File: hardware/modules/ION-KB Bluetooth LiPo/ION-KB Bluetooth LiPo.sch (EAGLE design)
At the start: 4 parts, among them IC1 BLUETOOTH-RN42", U1 MCP73831

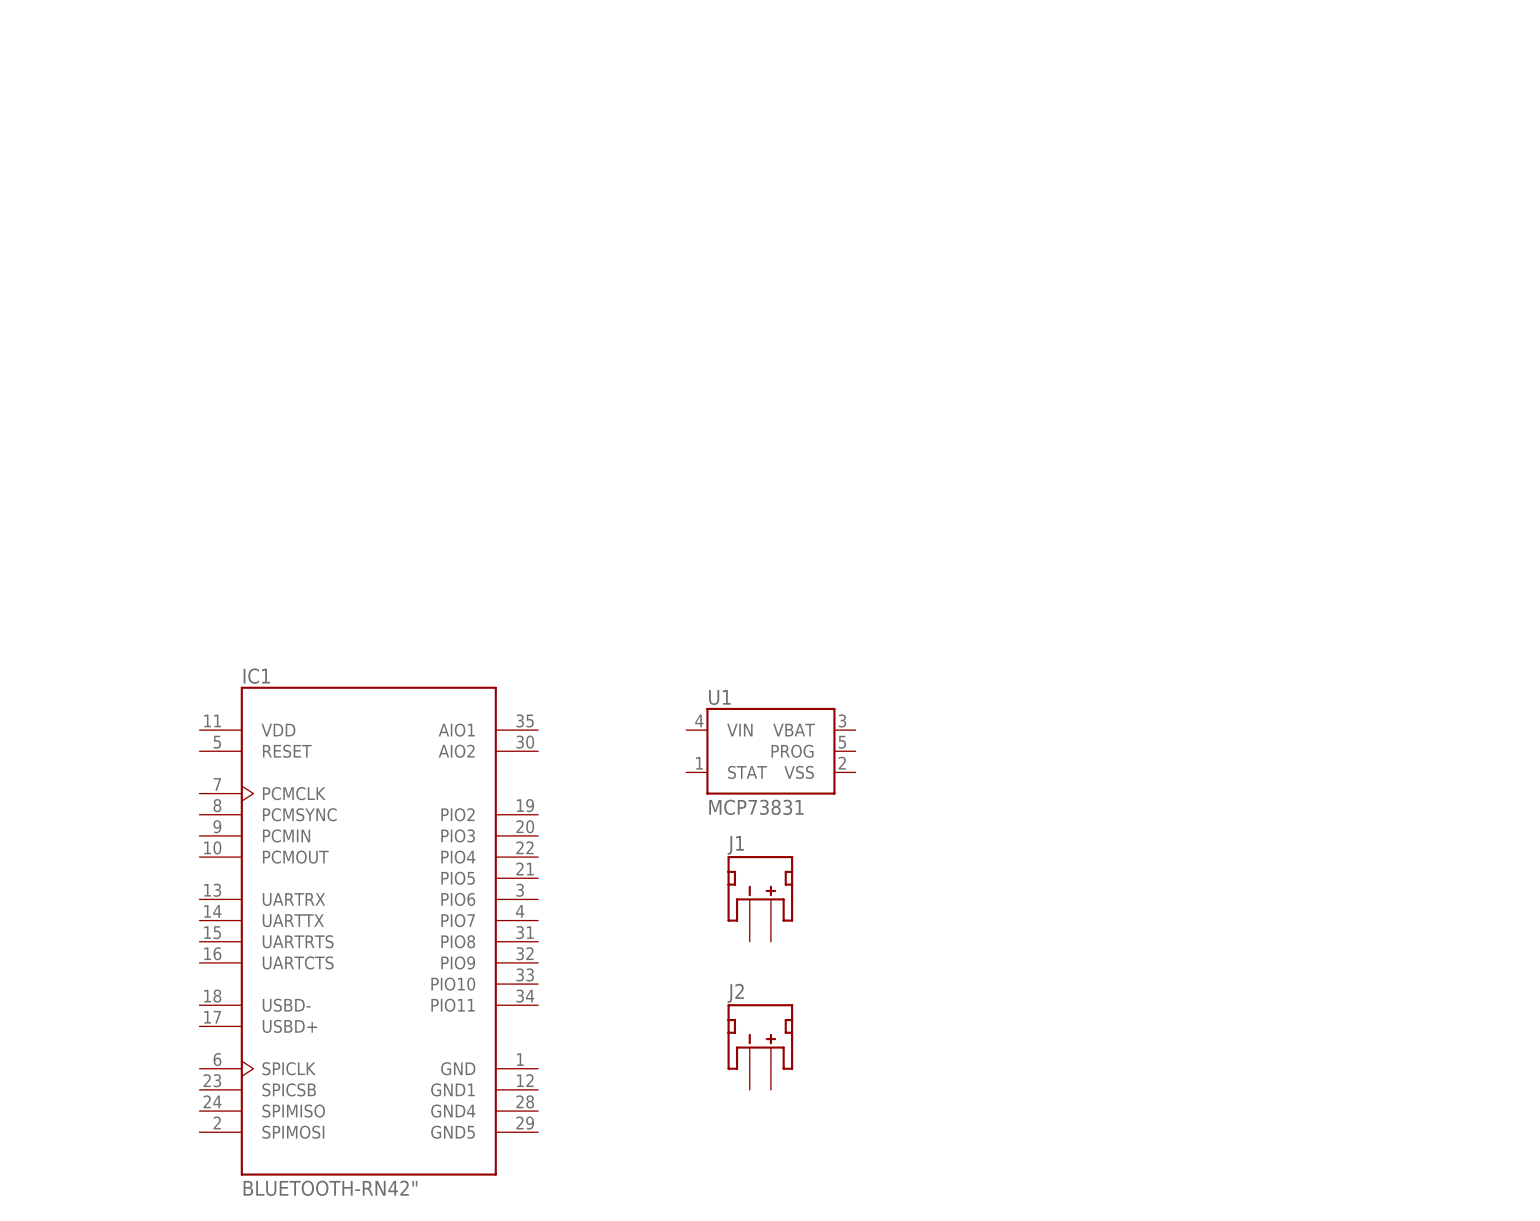
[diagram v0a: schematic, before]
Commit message: Update bluetooth module
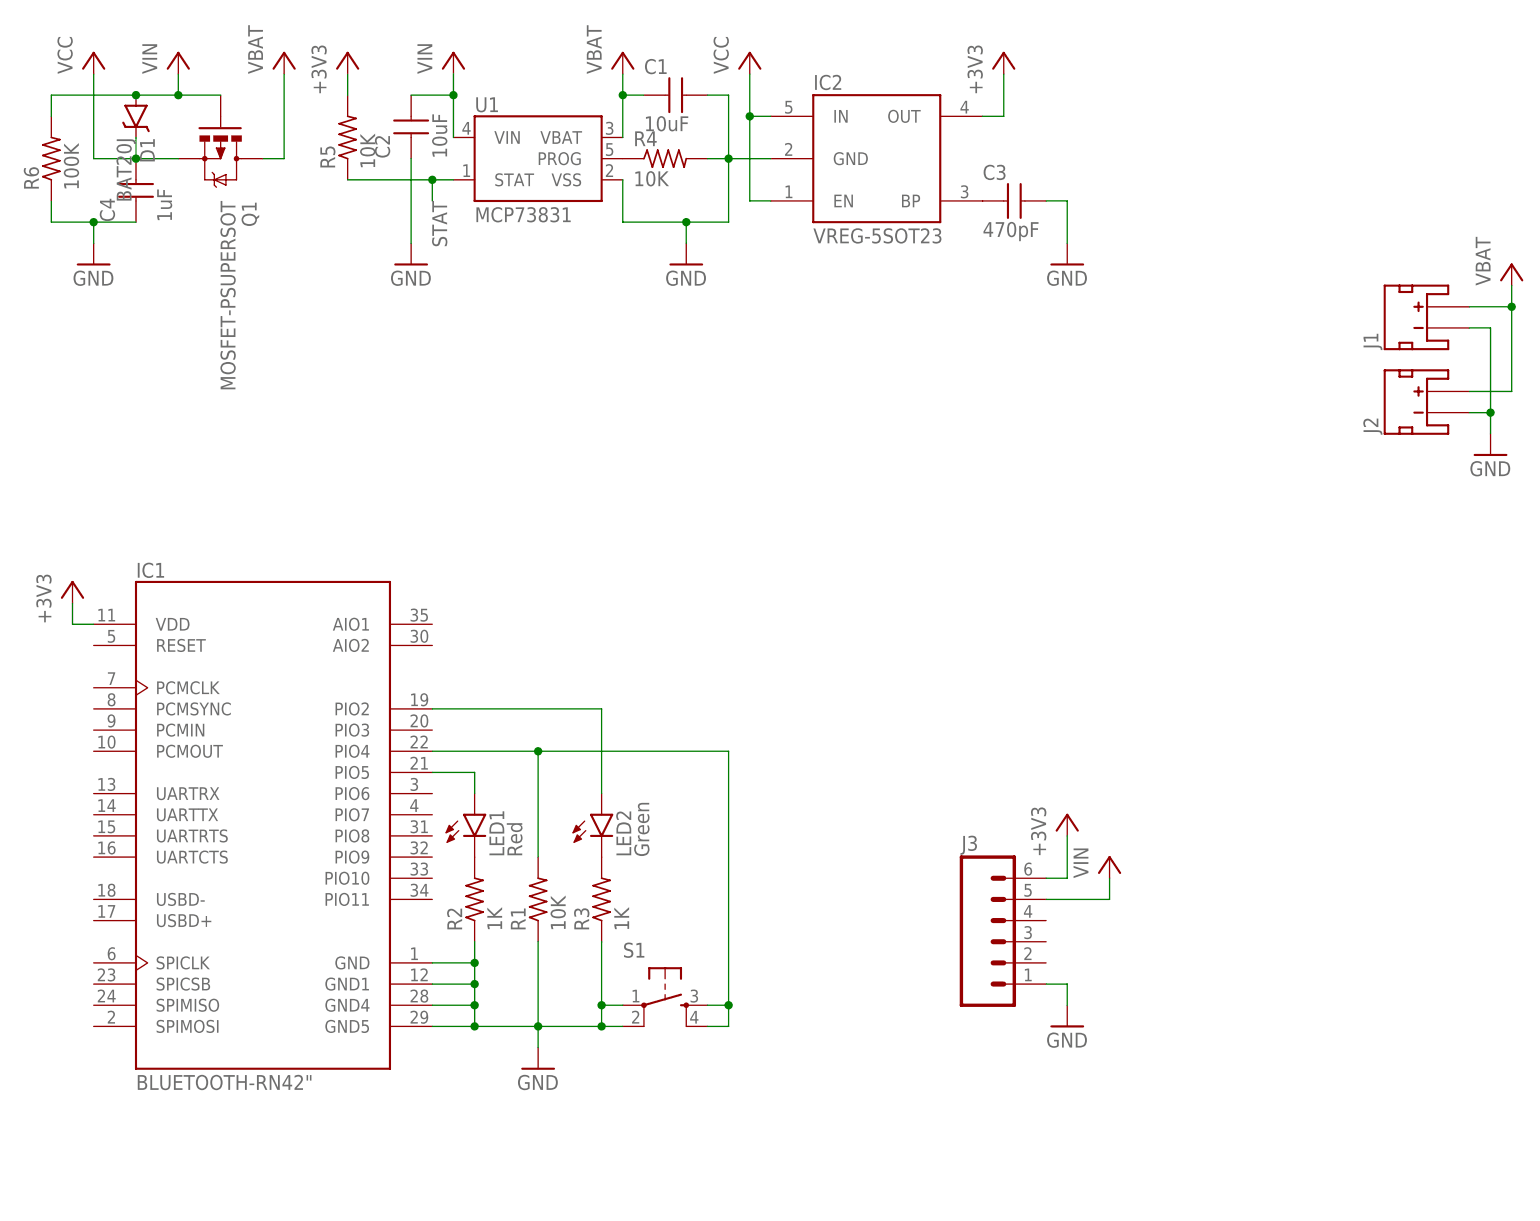
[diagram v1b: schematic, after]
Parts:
- added C1, C2: 10uF, Jordi:CAPACITOR0603
- added C3: 470pF, Jordi:CAPACITOR0603
- added C4: 1uF, Jordi:CAPACITOR0603
- added D1: BAT20J, SparkFun-DiscreteSemi:DIODE-SCHOTTKY-BAT20J
- added IC2: VREG-5SOT23, Jordi:VREG-5SOT23
- added J3: (no value), Jordi:1X06M-0.05-PTH
- added LED1: Red, Jordi:LED0603
- added LED2: Green, Jordi:LED0603
- added Q1: MOSFET-PSUPERSOT, Jordi:MOSFET-PSUPERSOT
- added R1, R4, R5: 10K, Jordi:RESISTOR0603
- added R2, R3: 1K, Jordi:RESISTOR0603
- added R6: 100K, Jordi:RESISTOR0603
- added S1: (no value), Jordi:SWITCH-TACTILESMD
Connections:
- new net +3V3: IC1.VDD, IC2.OUT, J3.6, R5.2
- new net GND: C1.2, C2.1, C3.2, C4.1, IC1.GND, IC1.GND1, IC1.GND4, IC1.GND5, IC2.GND, J1.-, J2.-, J3.1, R1.1, R2.1, R3.1, R4.2, R6.1, S1.1, S1.2, U1.VSS
- new net N$1: IC1.PIO4, R1.2, S1.3, S1.4
- new net N$2: LED1.C, R2.2
- new net N$3: IC1.PIO5, LED1.A
- new net N$4: IC1.PIO2, LED2.A
- new net N$5: LED2.C, R3.2
- new net N$6: R4.1, U1.PROG
- new net N$8: C3.1, IC2.BP
- new net STAT: R5.1, U1.STAT
- new net VBAT: C1.1, J1.+, J2.+, Q1.D, U1.VBAT
- new net VCC: C4.2, D1.C, IC2.EN, IC2.IN, Q1.S
- new net VIN: C2.2, D1.A, J3.5, Q1.G, R6.2, U1.VIN
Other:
- moved on the sheet: IC1, J1, J2, U1

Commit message: Remove VREG from Bluetooth board
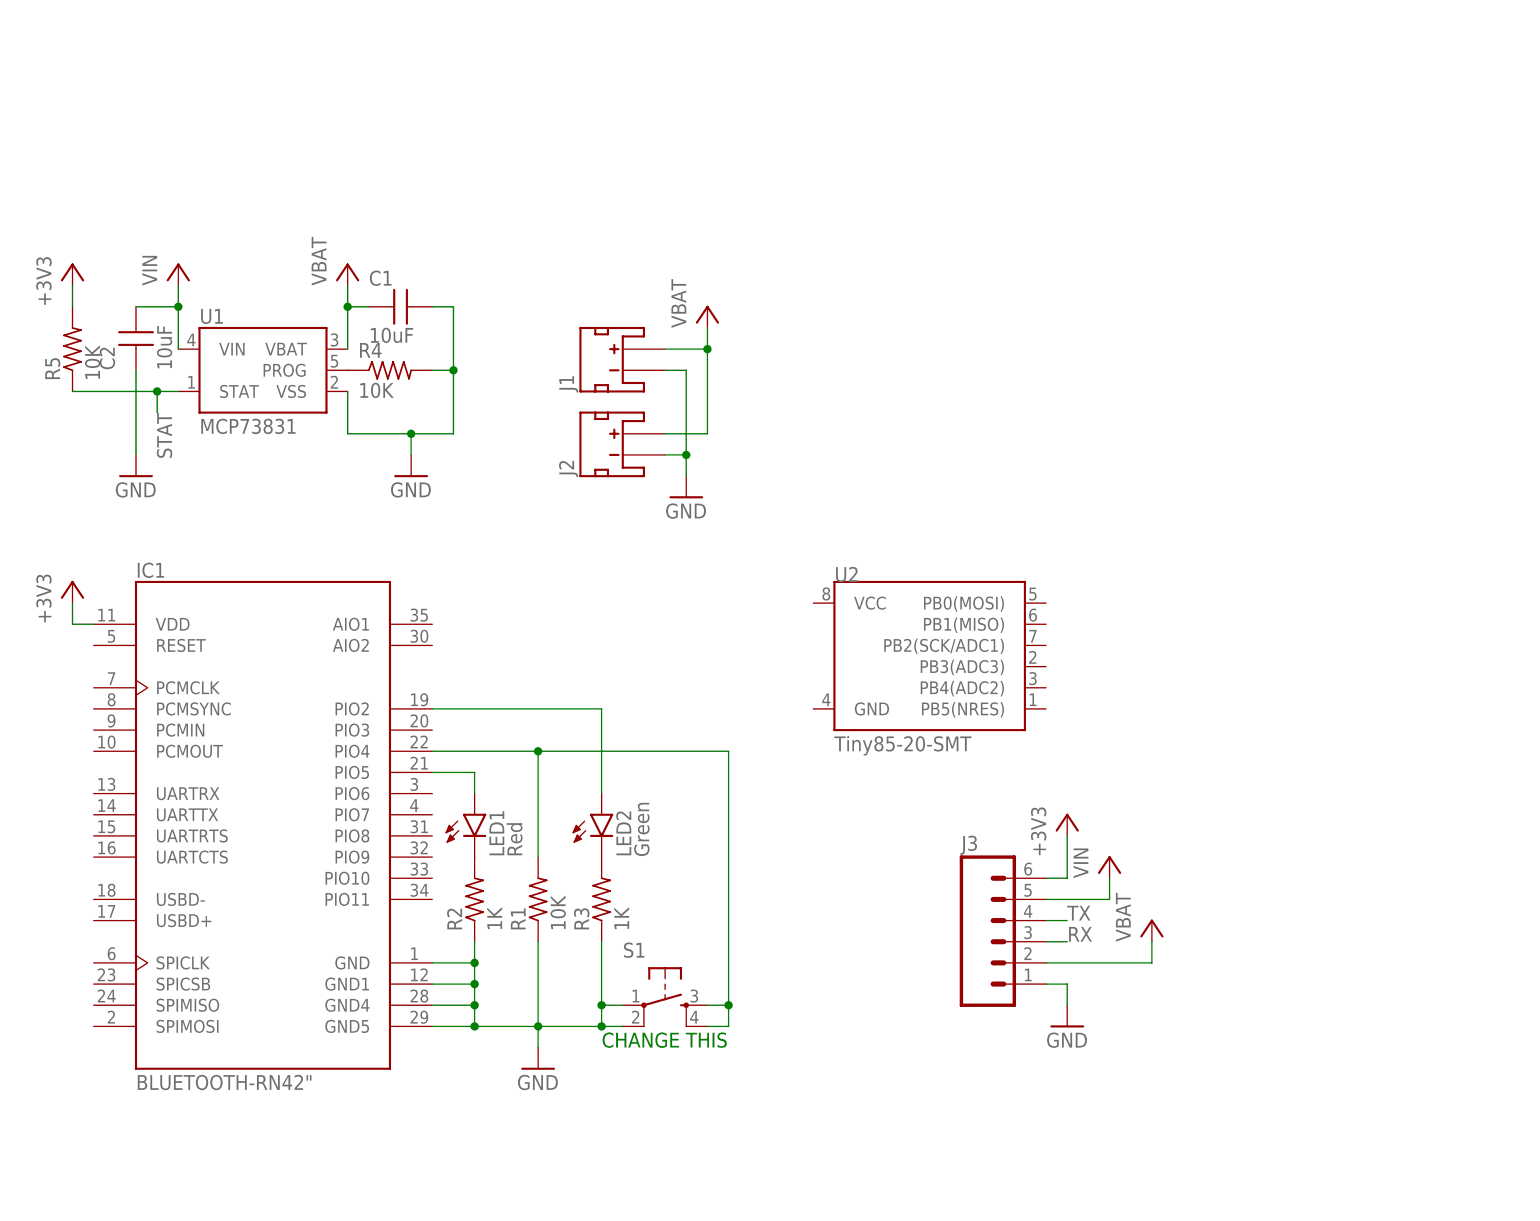
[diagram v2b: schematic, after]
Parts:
- removed C3: 470pF, Jordi:CAPACITOR0603
- removed C4: 1uF, Jordi:CAPACITOR0603
- removed D1: BAT20J, SparkFun-DiscreteSemi:DIODE-SCHOTTKY-BAT20J
- removed IC2: VREG-5SOT23, Jordi:VREG-5SOT23
- removed Q1: MOSFET-PSUPERSOT, Jordi:MOSFET-PSUPERSOT
- removed R6: 100K, Jordi:RESISTOR0603
- added U2: Tiny85-20-SMT, SparkFun-DigitalIC:ATTINY45TINY85-20-SMT
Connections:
- removed net N$8: C3.1, IC2.BP
- removed net VCC: C4.2, D1.C, IC2.EN, IC2.IN, Q1.S
- new net RX: J3.3
- new net TX: J3.4
- net +3V3: no longer IC2.OUT
- net GND: no longer C3.2, C4.1, IC2.GND, R6.1
- net VBAT: now also J3.2; no longer Q1.D
- net VIN: no longer D1.A, Q1.G, R6.2
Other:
- note added: "CHANGE THIS"
- moved on the sheet: C1, C2, J1, J2, R4, R5, U1
